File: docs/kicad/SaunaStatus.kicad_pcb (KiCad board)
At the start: 2 copper layers, 153 x 101 mm, 9 parts, among them J1 Adafruit-MAX31865-Breakout, J2 28BYJ-48, J3 28BYJ-48, J4 DHT21/AM2301 Ceiling, J5 DHT21/AM2301 Bench, U1 ESP32-WROOM-32, U5 ULN2003A, U6 ULN2003A, U7 INA260

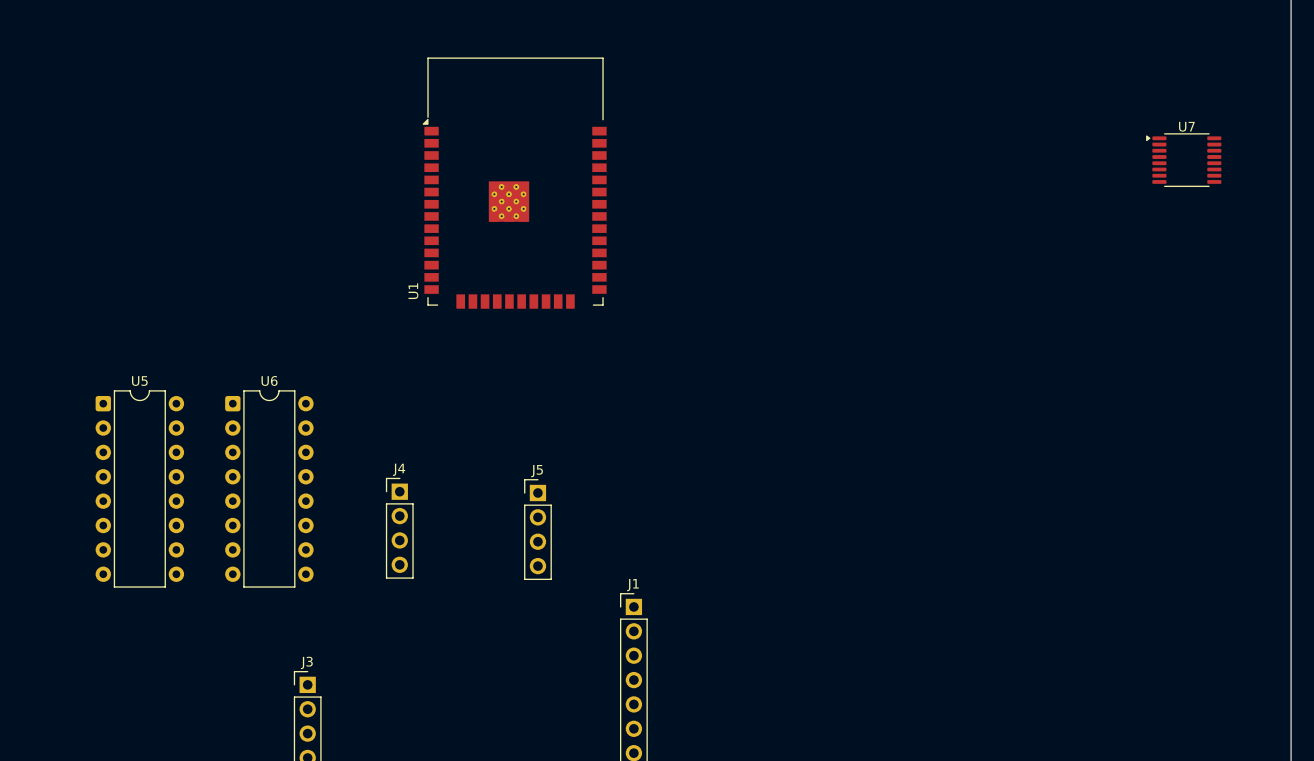
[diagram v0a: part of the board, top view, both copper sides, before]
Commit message: feat(kicad): replace bare IC symbols/footprints with breakout board connectors
Replace U1 (ESP32-WROOM-32), U5/U6 (ULN2003A DIP-16), and U7 (INA260
TSSOP-16) bare IC symbols in the schematic with connector symbols that
match the physical breakout boards used in the build:

- U1 → esp32_devkit_v1_doit (2×15 through-hole header)
- U5/U6 → J_*_IN (Conn_01x07) + J_*_OUT (Conn_01x04) + J_*_PWR
          (Conn_01x02) representing ULN2003A-PCB breakout connectors
- U7 → J_U7_SIG (Conn_01x08) + J_U7_CUR (Conn_01x02) representing
       Adafruit INA260 PCB breakout connectors

PCB updated to match: bare SMD/DIP footprints replaced with PinHeader
stubs. 55 pytest tests in test/test_kicad_connectors.py verify net
preservation, symbol replacement, and PCB footprint replacement.
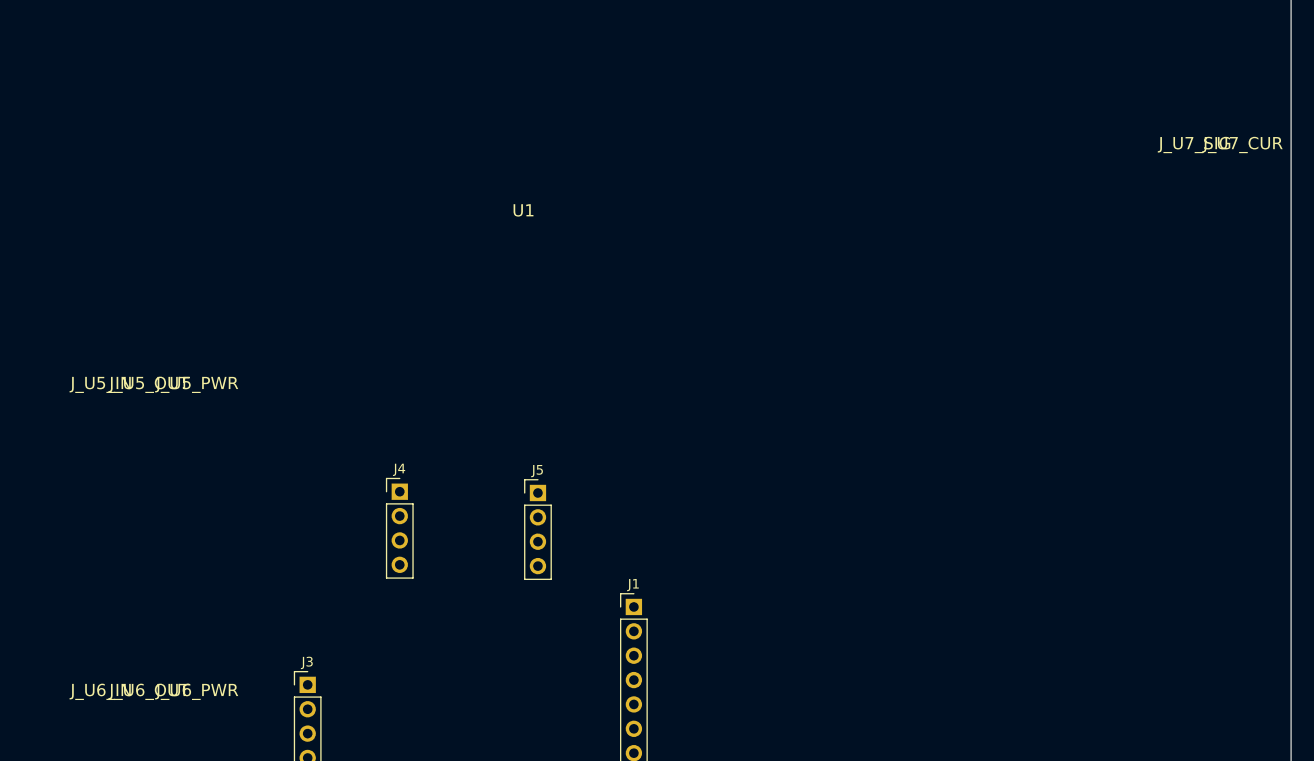
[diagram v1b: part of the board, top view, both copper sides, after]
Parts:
- removed U5, U6: ULN2003A, Package_DIP:DIP-16_W7.62mm
- removed U7: INA260, Package_SO:TSSOP-16_4.4x5mm_P0.65mm
- added J_U5_IN: ULN2003A-IN, Connector_PinHeader_2.54mm:PinHeader_1x07_P2.54mm_Vertical, F.Cu at (96.0, 88.0)
- added J_U5_OUT: ULN2003A-OUT, Connector_PinHeader_2.54mm:PinHeader_1x04_P2.54mm_Vertical, F.Cu at (101.0, 88.0)
- added J_U5_PWR: ULN2003A-PWR, Connector_PinHeader_2.54mm:PinHeader_1x02_P2.54mm_Vertical, F.Cu at (106.0, 88.0)
- added J_U6_IN: ULN2003A-IN, Connector_PinHeader_2.54mm:PinHeader_1x07_P2.54mm_Vertical, F.Cu at (96.0, 120.0)
- added J_U6_OUT: ULN2003A-OUT, Connector_PinHeader_2.54mm:PinHeader_1x04_P2.54mm_Vertical, F.Cu at (101.0, 120.0)
- added J_U6_PWR: ULN2003A-PWR, Connector_PinHeader_2.54mm:PinHeader_1x02_P2.54mm_Vertical, F.Cu at (106.0, 120.0)
- added J_U7_CUR: INA260-X1, Connector_PinHeader_2.54mm:PinHeader_1x02_P2.54mm_Vertical, F.Cu at (215.0, 63.0)
- added J_U7_SIG: INA260-JP2, Connector_PinHeader_2.54mm:PinHeader_1x08_P2.54mm_Vertical, F.Cu at (210.0, 63.0)
- U1: value ESP32-WROOM-32 -> ESP32-DevKit-V1-DOIT; footprint RF_Module:ESP32-WROOM-32 -> Connector_PinHeader_2.54mm:PinHeader_2x15_P2.54mm_Vertical
- moved U1 2.21 mm to (140.0, 70.0)
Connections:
- J1 pad 1: (no net) -> +3V3
- J1 pad 2: (no net) -> unconnected-(J1-Pin_2-Pad2)
- J1 pad 3: (no net) -> GND
- J1 pad 4: (no net) -> /SPI_SCK
- J1 pad 5: (no net) -> /SPI_MISO
- J1 pad 6: (no net) -> /SPI_MOSI
- J1 pad 7: (no net) -> /SPI_CS
- J1 pad 8: (no net) -> unconnected-(J1-Pin_8-Pad8)
- J3 pad 1: unconnected-(J3-Pin_1-Pad1) -> /U6_28BYJ_A
- J3 pad 2: unconnected-(J3-Pin_2-Pad2) -> /U6_28BYJ_B
- J4 pad 1: unconnected-(J4-Pin_1-Pad1) -> +3V3
- J4 pad 4: unconnected-(J4-Pin_4-Pad4) -> GND
- J5 pad 1: unconnected-(J5-Pin_1-Pad1) -> +3V3
- J5 pad 4: unconnected-(J5-Pin_4-Pad4) -> GND

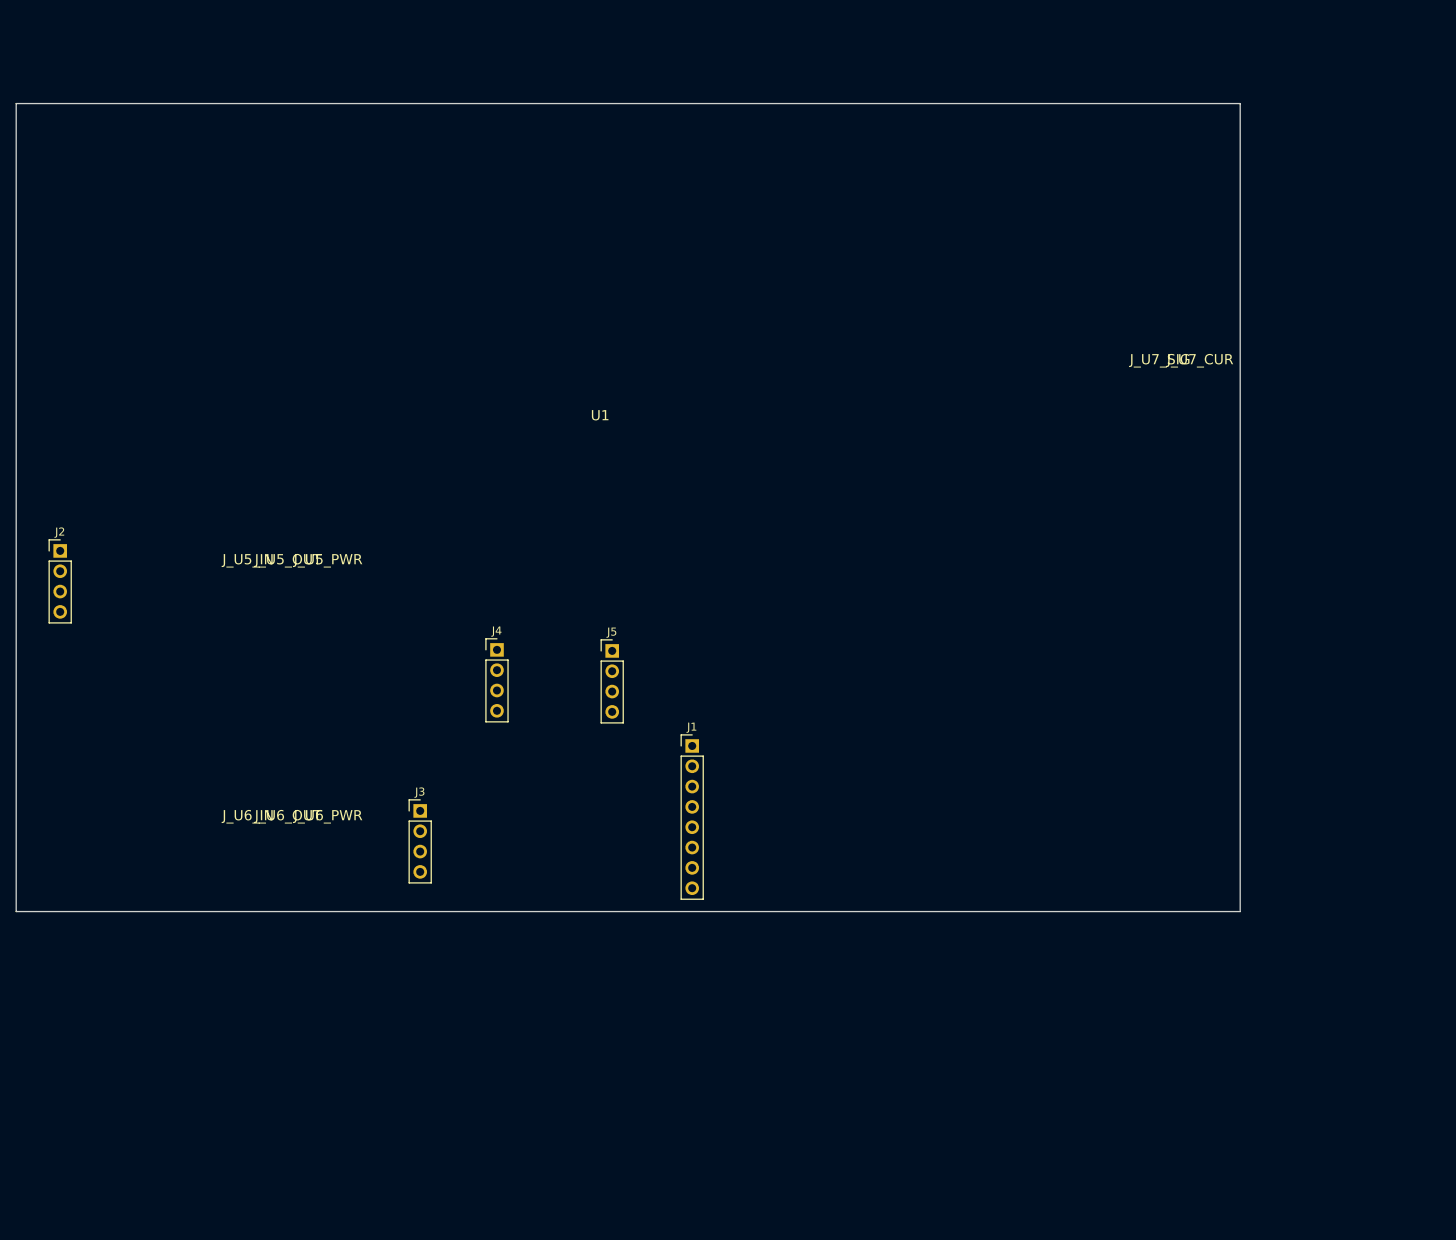
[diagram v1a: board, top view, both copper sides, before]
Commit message: feat(hw): migrate from ESP32-DevKit to LB-ESP32S3-N16R8 (ESP32-S3)
Board migration to LB-ESP32S3-N16R8 (Lolin S3 form factor, ESP32-S3
N16R8 — 16 MB OPI flash, 8 MB PSRAM). All GPIO assignments verified
against physical board and unit-tested.

Firmware changes:
- src/gpio_config.h: new header centralising all GPIO #defines for
  ESP32-S3 (SPI, I2C, DHT, outflow/inflow motor pins); replaces
  scattered literals in main.cpp
- src/main.cpp: updated pin assignments to ESP32-S3 GPIOs; added
  gpio_config.h include
- platformio.ini: added lb_esp32s3 environment (lolin_s3 board, OPI
  memory type, 16 MB partition table); upesy_wroom kept as legacy
  reference; lb_esp32s3 is now default
- partitions_ota_16mb.csv: new 16 MB OTA partition table (spiffs
  partition named "spiffs" per LittleFS.begin() requirement)

Tests:
- test/test_gpio_config/test_main.cpp: 21 native unit tests covering
  pin values, adjacency, conflicts, restricted-pin exclusions, motor
  coil order, and valid-range assertions

KiCad schematic:
- docs/kicad/SaunaStatus.kicad_sch: removed U1 ESP32-DevKit-V1-DOIT
  symbol; replaced with J_LEFT / J_RIGHT Conn_01x20 breakout-board
  header connectors with net labels (OUTFLOW_I1–I4, INFLOW_I1–I4,
  SPI_*, I2C_*, DHT_*, +3V3, GND) and no-connect marks on unused pins
- docs/kicad/SaunaStatus.kicad_pcb: updated PCB to match schematic
- docs/datasheets/LB-ESP32S3-N16R8-Pinout-Modifed/: KiCad footprint
  for LB-ESP32S3-N16R8 (2×20 through-hole, 2.54 mm pitch)

Docs:
- docs/pinout.md: updated GPIO table for ESP32-S3 assignments
- CLAUDE.md: updated build commands (pio run -t build vs upload
  distinction, both-upload warning), compacted unit-test section to
  summary table, removed stale cross-reference
- .claude/settings.local.json: updated tool permissions

GPIO35–38 appear on the board header (SPIIO6/7, SPIDQS, FSPIWP) but
may be internally connected to the OPI flash interface — treated as
reserved in gpio_config.h and test assertions.
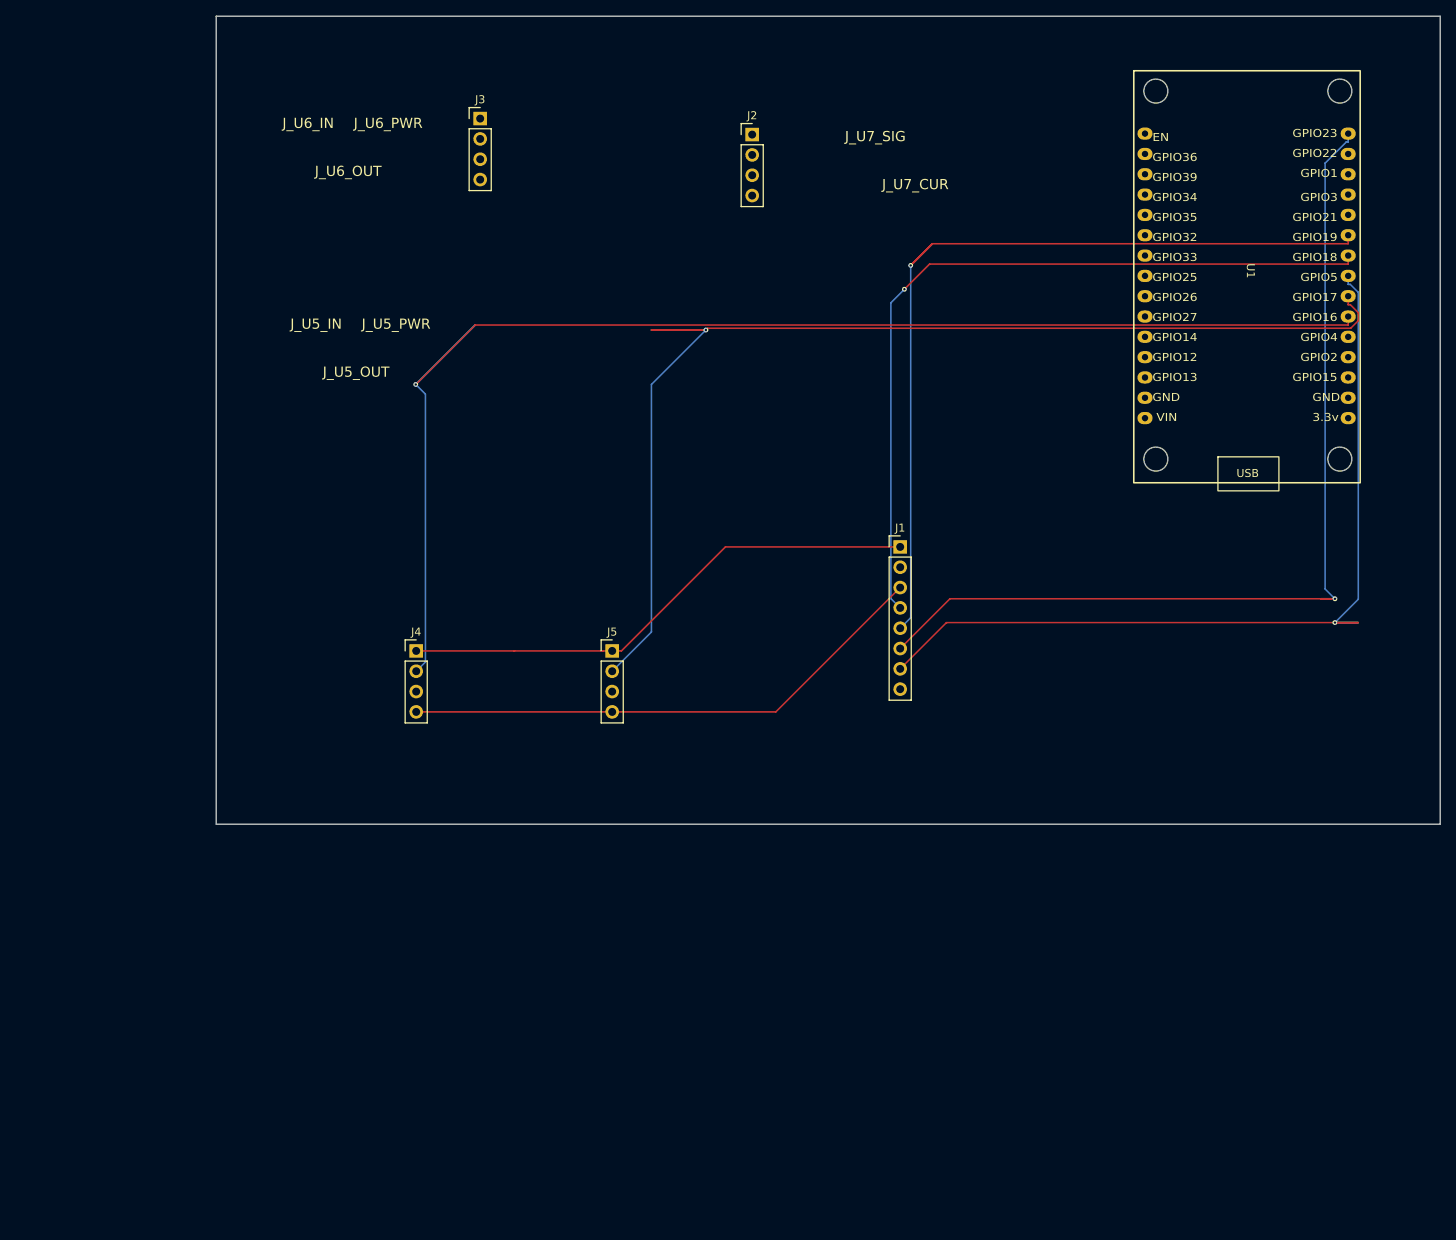
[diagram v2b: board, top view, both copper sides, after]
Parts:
- U1: footprint Connector_PinHeader_2.54mm:PinHeader_2x15_P2.54mm_Vertical -> ESP32_Footprints:ESP32_30pin
- moved J2 100.9 mm to (159.0, 32.9)
- moved J3 86.9 mm to (125.0, 30.9)
- moved J_U6_IN 86.9 mm to (103.5, 33.5)
- moved J_U6_OUT 86.9 mm to (108.5, 33.5)
- moved J_U6_PWR 86.9 mm to (113.5, 33.5)
- moved U1 82.2 mm to (220.0, 51.3)
- moved J_U7_CUR 45.2 mm to (179.4, 35.1)
- moved J_U7_SIG 45.2 mm to (174.4, 35.1)
- moved J1 36.0 mm to (177.5, 84.4)
- moved J_U5_IN 30.6 mm to (104.5, 58.6)
- moved J_U5_OUT 30.6 mm to (109.5, 58.6)
- moved J_U5_PWR 30.6 mm to (114.5, 58.6)
- moved J4 10.1 mm to (117.0, 97.4)
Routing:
- net /DHT_CEILING: track 0.00 -> 178.5 mm, vias 0 -> 1
- net /DHT_BENCH: track 0.00 -> 160.5 mm, vias 0 -> 1
- net /SPI_MOSI: track 0.00 -> 123.9 mm, vias 0 -> 1
- net /SPI_MISO: track 0.00 -> 118.1 mm, vias 0 -> 1
- net /SPI_CS: track 0.00 -> 113.6 mm, vias 0 -> 1
- net /SPI_SCK: track 0.00 -> 99.8 mm, vias 0 -> 1
- net GND: track 0.00 -> 66.9 mm
- net +3V3: track 0.00 -> 65.9 mm
